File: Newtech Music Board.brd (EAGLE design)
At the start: 133.3 x 79.7 mm, 56 parts, among them IC1 LM386N-1, J1 SS-30_BOARD_CONNECTOR, J2 MJ-3502N, U1 74LS10N, U2 74LS174N, U3 4050N, U4 4069N, U6 78L05

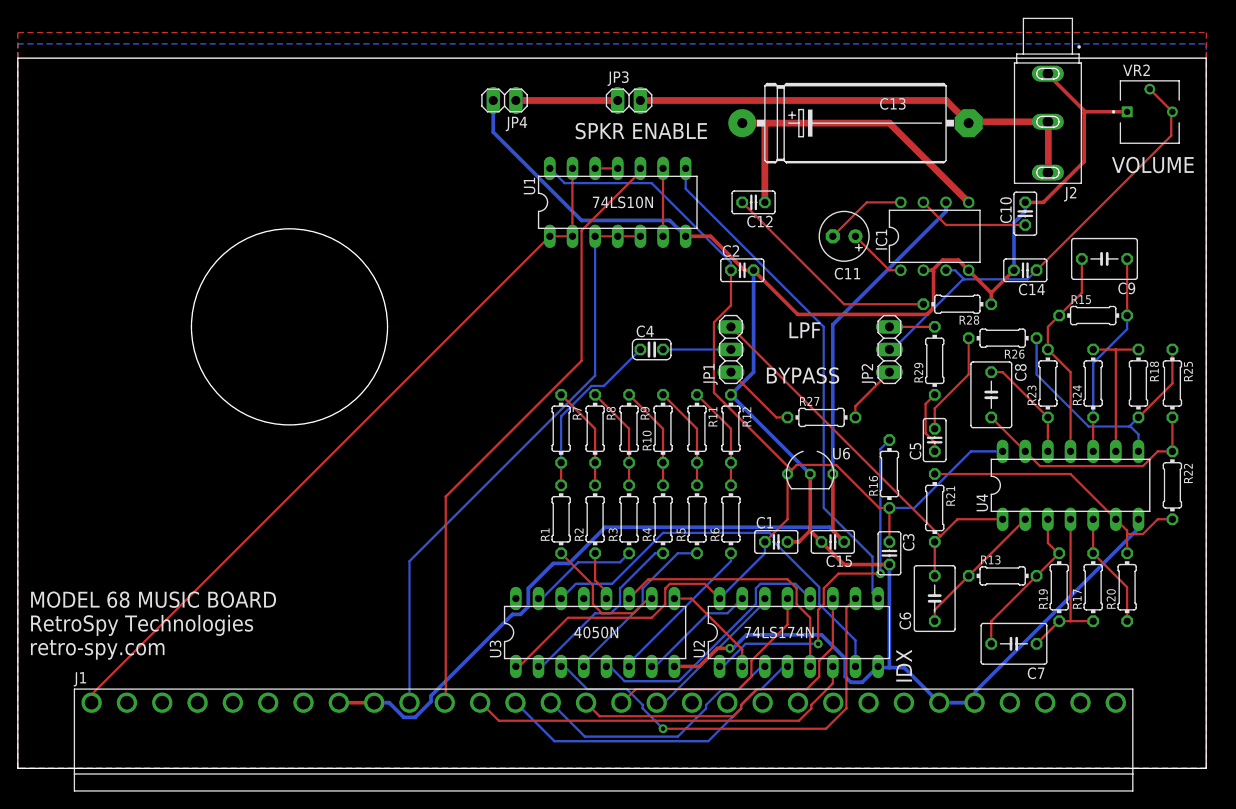
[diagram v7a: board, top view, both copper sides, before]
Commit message: Rearranged ICs to try and fix stuttering
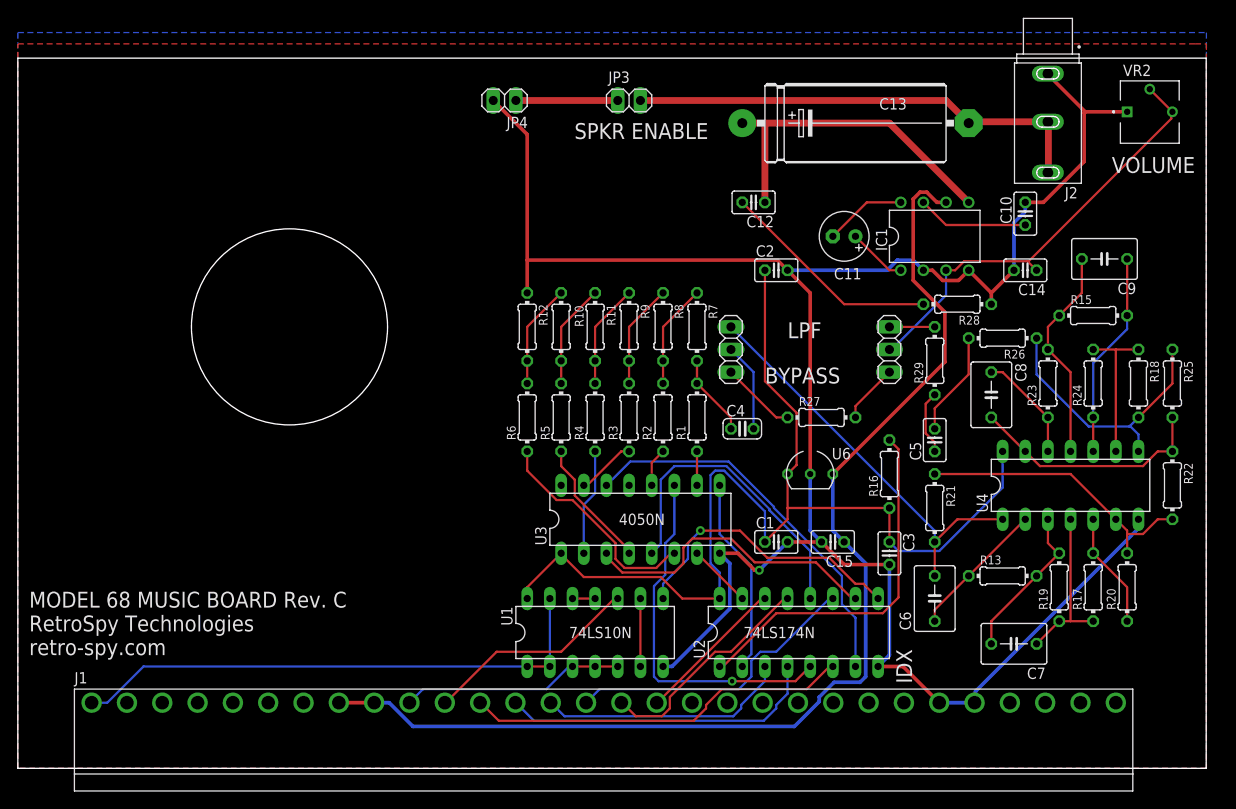
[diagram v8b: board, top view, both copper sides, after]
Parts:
- moved U1 48.3 mm to (64.8, 15.2)
- moved R12 25.6 mm to (57.1, 49.5)
- moved R6 25.6 mm to (57.1, 39.4)
- moved R11 19.1 mm to (61.0, 49.5)
- moved R7 19.1 mm to (76.2, 49.5)
- moved R1 19.1 mm to (76.2, 39.4)
- moved R5 19.1 mm to (61.0, 39.4)
- moved R10 13.7 mm to (64.8, 49.5)
- moved R8 13.7 mm to (72.4, 49.5)
- moved R2 13.7 mm to (72.4, 39.4)
- moved R4 13.7 mm to (64.8, 39.4)
- moved U3 13.7 mm to (69.8, 27.9)
- moved C4 13.5 mm to (81.3, 38.1)
- moved R9 11.4 mm to (68.6, 49.5)
- moved R3 11.4 mm to (68.6, 39.4)
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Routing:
- net PHASE2: track 69.1 -> 24.2 mm
- net R/!W: track 66.0 -> 25.1 mm
- net N$16: track 57.2 -> 32.5 mm, vias 0 -> 1
- net !SELECT: track 83.8 -> 60.7 mm
- net +8V: track 112.3 -> 129.1 mm
- net N$12: track 48.8 -> 34.5 mm, vias 1 -> 0
- net N$10: track 29.5 -> 40.8 mm, vias 0 -> 1
- net N$18: track 14.9 -> 3.81 mm
- net N$29: track 19.7 -> 9.20 mm
- net N$9: track 11.9 -> 22.2 mm
- net +5V: track 130.9 -> 121.3 mm
- net N$21: track 20.3 -> 12.0 mm
- net N$23: track 17.4 -> 24.9 mm
- net N$14: track 13.3 -> 7.18 mm
- net N$13: track 29.8 -> 35.4 mm
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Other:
- board text added: "MODEL 68 MUSIC BOARD Rev. C RetroSpy Technologies retro-spy.com"
- board text removed: "MODEL 68 MUSIC BOARD RetroSpy Technologies retro-spy.com"
